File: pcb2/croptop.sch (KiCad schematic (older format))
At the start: 0 parts

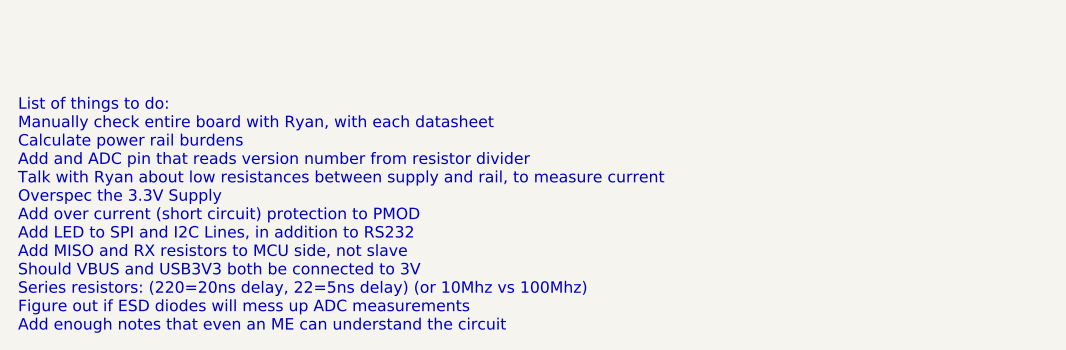
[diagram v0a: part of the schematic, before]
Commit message: Added USB port control
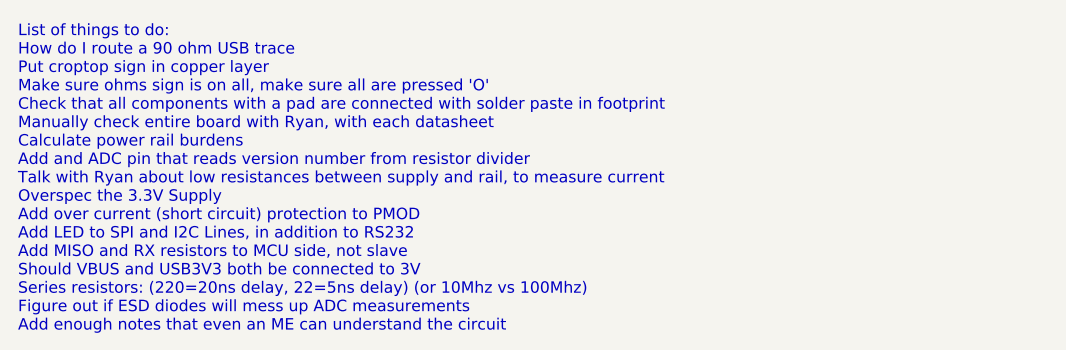
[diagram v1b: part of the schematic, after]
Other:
- note added: "List of things to do:\nHow do I route a 90 ohm USB trace\nPut croptop sign in copper layer\nMake sure ohms sign is on all, make sure all are pressed 'O'\nCheck that all components with a pad are connected with solder paste in footprint\nManually check entire board with Ryan, with each datasheet\nCalculate power rail burdens\nAdd and ADC pin that reads version number from resistor divider\nTalk wi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"
- note removed: "List of things to do:\nManually check entire board with Ryan, with each datasheet\nCalculate power rail burdens\nAdd and ADC pin that reads version number from resistor divider\nTalk with Ryan about low resistances between supply and rail, to measure current\nOverspec the 3.3V Supply\nAdd over current (short circuit) protection to PMOD\nAdd LED to SPI and I2C Lines, in addition to RS232\nAdd MISO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"
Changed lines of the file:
@@
 System Block Diagram
 Text Notes 1250 7850 0    50   ~ 0
-List of things to do:\nManually check entire board with Ryan, with each datasheet\nCalculate power rail burdens\nAdd and ADC pin that reads version number from resistor divider\nTalk with Ryan about low resistances between supply and rail, to measure current\nOverspec the 3.3V Supply\nAdd over current (short circuit) protection to PMOD\nAdd LED to SPI and I2C Lines, in addition to RS232\nAdd MISO and RX resistors to MCU side, not slave\nShould VBUS and USB3V3 both be connected to 3V\nSeries resistors: (220=20ns delay, 22=5ns delay) (or 10Mhz vs 100Mhz)\nFigure out if ESD diodes will mess up ADC measurements\nAdd enough notes that even an ME can understand the circuit\n\nImplement all 4 types of protection:\nReverse polarity protection: PMOS\nFOLLOW PCB Layout tips (temp, GPS, etc)\nAdd a ground pour to empty planes\nESD protection: TVS diodes\nOvervoltage protection: Buffers and schokttky diodes\nOvercurrent protection: PTC fuses AND eFuses\ndv/dt (rise time) protection: series diodes\nRC filters on the input\nLook into Chris Gammel's powerpoint for more info\n\nCome up with different devices configurations (using DNP for components)\n5 Terminal block pins were used for each force sensor\nDoes DRV_FLT need a pull up?\nLook into thermal vias for motor drivers\nAdd silkscreen labels to configuration resistors\nAdd address of components to sheet\nMore protection on motor and stepper? (Stepper pg. 15)\nMake location of resistor value consistent (inside vs. outside)\nMake sure all devices have testpoint in any useful places\nWhen laying out the footprint for the motor drivers, follow datasheet\nRe add isolation dotted box around ADI ADC\nRemove electrolytic input on DC motor driver\nChange AVDD to 5V0_REG, DVDD to 3V3\nAdd inductor to ADC\nChange nets to have directions\nRemove global nets on power\nAdd missing pullups and pulldowns on temp/memory\nAdd MISO to SPI bus\nAdd resistor to Load bank for current limit\nMake board larger at top, add header blocks\nRemove electrolytic input on DC motor driver\nChange AVDD to 5V0_REG, DVDD to 3V3\nCheck regulators can carry high current\nMove micro usb and lcd connector further forward\nSplit memory and adc spi bus\nFlip direction of motor diode\nMap out extra I2C and SPI busses to terminal blocks\nAdd a stepper motor driver\nAdd heat sinks to motor drivers\nRun through pin out of every chip and verify it's connection\nVerify the package footprint of every chip\nAdd ground plane to top and bottom layers\nStitch top and bottom layers together with vias\nAdd pullup resistors/pulldown resistors to data lines\nAdd a second USB port\nAdd a USB switch: USB2422\nAdd a UART to USB coverter: FT232RQ\nAdd LEDs to communication channels\nAdd Series resistors to comm lines, allowing the resistor to be changed\nAdd A4988 stepper motor driver\nAdd GPIO Block with ESD protection\nAdd SPI/UART/I2C with ESD potection on terminal blocks\nAdd labels to terminal blocks, on underside\nThroughole USB\nGround plane on top and bottom layer\nAdd configurable voltage to IO ports\nMove testpoints onto schematic\nPut I2C address on I2C chips\nMake sure all global nets are facing right direciton\nMake sure all LED resistors are selected\nSPI I2C and RS232 testpoints should be closer to pic, or at fork point\nCheck if DC and Stepper motor needs external flyback diodes\nAll elements that have a pad, make sure that there is a pad pin and it's footprint is has the pad assigned to it\nMake sure all CAP on motor drivers are at least 50V Rated\nChange name of I2C and SPI and RS232 to add numbers and what bus? (tx -> I2C_TX_1)\nMove memory and ADC to different busses\nAdd datasheets for components into schematic\nMake sure that 3V3 rotary encoder buffer resistor is DNP\nLabel Terminal blocks on top side\nChange accellerometer to gyro L3GD20H\nRemove buffer from ADC\nMove ADC over star ground\nFigure out whether off board peripherals need buffer\nGive all devices a 10uF and 0.1uF (100nF) capacitor, at the very least\nCan Stepper motor driver use 3.3V for REF?\nAdd an audio circuit to the FTDI chip (recommends TPA6205A1)\nMove ADC and NAND to different SPI Buses\nMake NAND 1GB instead of 1Gb\n\n\n\n
+List of things to do:\nHow do I route a 90 ohm USB trace\nPut croptop sign in copper layer\nMake sure ohms sign is on all, make sure all are pressed 'O'\nCheck that all components with a pad are connected with solder paste in footprint\nManually check entire board with Ryan, with each datasheet\nCalculate power rail burdens\nAdd and ADC pin that reads version number from resistor divider\nTalk with Ryan about low resistances between supply and rail, to measure current\nOverspec the 3.3V Supply\nAdd over current (short circuit) protection to PMOD\nAdd LED to SPI and I2C Lines, in addition to RS232\nAdd MISO and RX resistors to MCU side, not slave\nShould VBUS and USB3V3 both be connected to 3V\nSeries resistors: (220=20ns delay, 22=5ns delay) (or 10Mhz vs 100Mhz)\nFigure out if ESD diodes will mess up ADC measurements\nAdd enough notes that even an ME can understand the circuit\n\nImplement all 4 types of protection:\nReverse polarity protection: PMOS\nFOLLOW PCB Layout tips (temp, GPS, etc)\nAdd a ground pour to empty planes\nESD protection: TVS diodes\nOvervoltage protection: Buffers and schokttky diodes\nOvercurrent protection: PTC fuses AND eFuses\ndv/dt (rise time) protection: series diodes\nRC filters on the input\nLook into Chris Gammel's powerpoint for more info\n\nCome up with different devices configurations (using DNP for components)\n5 Terminal block pins were used for each force sensor\nDoes DRV_FLT need a pull up?\nLook into thermal vias for motor drivers\nAdd silkscreen labels to configuration resistors\nAdd address of components to sheet\nMore protection on motor and stepper? (Stepper pg. 15)\nMake location of resistor value consistent (inside vs. outside)\nMake sure all devices have testpoint in any useful places\nWhen laying out the footprint for the motor drivers, follow datasheet\nRe add isolation dotted box around ADI ADC\nRemove electrolytic input on DC motor driver\nChange AVDD to 5V0_REG, DVDD to 3V3\nAdd inductor to ADC\nChange nets to have directions\nRemove global nets on power\nAdd missing pullups and pulldowns on temp/memory\nAdd MISO to SPI bus\nAdd resistor to Load bank for current limit\nMake board larger at top, add header blocks\nRemove electrolytic input on DC motor driver\nChange AVDD to 5V0_REG, DVDD to 3V3\nCheck regulators can carry high current\nMove micro usb and lcd connector further forward\nSplit memory and adc spi bus\nFlip direction of motor diode\nMap out extra I2C and SPI busses to terminal blocks\nAdd a stepper motor driver\nAdd heat sinks to motor drivers\nRun through pin out of every chip and verify it's connection\nVerify the package footprint of every chip\nAdd ground plane to top and bottom layers\nStitch top and bottom layers together with vias\nAdd pullup resistors/pulldown resistors to data lines\nAdd a second USB port\nAdd a USB switch: USB2422\nAdd a UART to USB coverter: FT232RQ\nAdd LEDs to communication channels\nAdd Series resistors to comm lines, allowing the resistor to be changed\nAdd A4988 stepper motor driver\nAdd GPIO Block with ESD protection\nAdd SPI/UART/I2C with ESD potection on terminal blocks\nAdd labels to terminal blocks, on underside\nThroughole USB\nGround plane on top and bottom layer\nAdd configurable voltage to IO ports\nMove testpoints onto schematic\nPut I2C address on I2C chips\nMake sure all global nets are facing right direciton\nMake sure all LED resistors are selected\nSPI I2C and RS232 testpoints should be closer to pic, or at fork point\nCheck if DC and Stepper motor needs external flyback diodes\nAll elements that have a pad, make sure that there is a pad pin and it's footprint is has the pad assigned to it\nMake sure all CAP on motor drivers are at least 50V Rated\nChange name of I2C and SPI and RS232 to add numbers and what bus? (tx -> I2C_TX_1)\nMove memory and ADC to different busses\nAdd datasheets for components into schematic\nMake sure that 3V3 rotary encoder buffer resistor is DNP\nLabel Terminal blocks on top side\nChange accellerometer to gyro L3GD20H\nRemove buffer from ADC\nMove ADC over star ground\nFigure out whether off board peripherals need buffer\nGive all devices a 10uF and 0.1uF (100nF) capacitor, at the very least\nCan Stepper motor driver use 3.3V for REF?\nAdd an audio circuit to the FTDI chip (recommends TPA6205A1)\nMove ADC and NAND to different SPI Buses\nMake NAND 1GB instead of 1Gb\n\n\n\n
 $Sheet
 S 7700 5150 1200 900

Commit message: Schematic near completion
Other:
- note added: "SCHEMATIC:\nShould Power rails be software or hardware enabled?\nMake sure ohms sign is on all, make sure all are pressed 'O'\nAdd and ADC pin that reads version number from resistor divider\nTalk with Ryan about low resistances between supply and rail, to measure current\nOverspec the 3.3V Supply\nAdd over current (short circuit) protection to PMOD\nAdd LED to SPI and I2C Lines, in addition to R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"
- note removed: "List of things to do:\nHow do I route a 90 ohm USB trace\nPut croptop sign in copper layer\nMake sure ohms sign is on all, make sure all are pressed 'O'\nCheck that all components with a pad are connected with solder paste in footprint\nManually check entire board with Ryan, with each datasheet\nCalculate power rail burdens\nAdd and ADC pin that reads version number from resistor divider\nTalk wi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"
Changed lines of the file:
@@
 $Descr USLetter 11000 8500
 encoding utf-8
-Sheet 1 7
+Sheet 1 6
 Title "CropTop"
 Date "2018-11-20"
@@
 System Block Diagram
 Text Notes 1250 7850 0    50   ~ 0
-List of things to do:\nHow do I route a 90 ohm USB trace\nPut croptop sign in copper layer\nMake sure ohms sign is on all, make sure all are pressed 'O'\nCheck that all components with a pad are connected with solder paste in footprint\nManually check entire board with Ryan, with each datasheet\nCalculate power rail burdens\nAdd and ADC pin that reads version number from resistor divider\nTalk with Ryan about low resistances between supply and rail, to measure current\nOverspec the 3.3V Supply\nAdd over current (short circuit) protection to PMOD\nAdd LED to SPI and I2C Lines, in addition to RS232\nAdd MISO and RX resistors to MCU side, not slave\nShould VBUS and USB3V3 both be connected to 3V\nSeries resistors: (220=20ns delay, 22=5ns delay) (or 10Mhz vs 100Mhz)\nFigure out if ESD diodes will mess up ADC measurements\nAdd enough notes that even an ME can understand the circuit\n\nImplement all 4 types of protection:\nReverse polarity protection: PMOS\nFOLLOW PCB Layout tips (temp, GPS, etc)\nAdd a ground pour to empty planes\nESD protection: TVS diodes\nOvervoltage protection: Buffers and schokttky diodes\nOvercurrent protection: PTC fuses AND eFuses\ndv/dt (rise time) protection: series diodes\nRC filters on the input\nLook into Chris Gammel's powerpoint for more info\n\nCome up with different devices configurations (using DNP for components)\n5 Terminal block pins were used for each force sensor\nDoes DRV_FLT need a pull up?\nLook into thermal vias for motor drivers\nAdd silkscreen labels to configuration resistors\nAdd address of components to sheet\nMore protection on motor and stepper? (Stepper pg. 15)\nMake location of resistor value consistent (inside vs. outside)\nMake sure all devices have testpoint in any useful places\nWhen laying out the footprint for the motor drivers, follow datasheet\nRe add isolation dotted box around ADI ADC\nRemove electrolytic input on DC motor driver\nChange AVDD to 5V0_REG, DVDD to 3V3\nAdd inductor to ADC\nChange nets to have directions\nRemove global nets on power\nAdd missing pullups and pulldowns on temp/memory\nAdd MISO to SPI bus\nAdd resistor to Load bank for current limit\nMake board larger at top, add header blocks\nRemove electrolytic input on DC motor driver\nChange AVDD to 5V0_REG, DVDD to 3V3\nCheck regulators can carry high current\nMove micro usb and lcd connector further forward\nSplit memory and adc spi bus\nFlip direction of motor diode\nMap out extra I2C and SPI busses to terminal blocks\nAdd a stepper motor driver\nAdd heat sinks to motor drivers\nRun through pin out of every chip and verify it's connection\nVerify the package footprint of every chip\nAdd ground plane to top and bottom layers\nStitch top and bottom layers together with vias\nAdd pullup resistors/pulldown resistors to data lines\nAdd a second USB port\nAdd a USB switch: USB2422\nAdd a UART to USB coverter: FT232RQ\nAdd LEDs to communication channels\nAdd Series resistors to comm lines, allowing the resistor to be changed\nAdd A4988 stepper motor driver\nAdd GPIO Block with ESD protection\nAdd SPI/UART/I2C with ESD potection on terminal blocks\nAdd labels to terminal blocks, on underside\nThroughole USB\nGround plane on top and bottom layer\nAdd configurable voltage to IO ports\nMove testpoints onto schematic\nPut I2C address on I2C chips\nMake sure all global nets are facing right direciton\nMake sure all LED resistors are selected\nSPI I2C and RS232 testpoints should be closer to pic, or at fork point\nCheck if DC and Stepper motor needs external flyback diodes\nAll elements that have a pad, make sure that there is a pad pin and it's footprint is has the pad assigned to it\nMake sure all CAP on motor drivers are at least 50V Rated\nChange name of I2C and SPI and RS232 to add numbers and what bus? (tx -> I2C_TX_1)\nMove memory and ADC to different busses\nAdd datasheets for components into schematic\nMake sure that 3V3 rotary encoder buffer resistor is DNP\nLabel Terminal blocks on top side\nChange accellerometer to gyro L3GD20H\nRemove buffer from ADC\nMove ADC over star ground\nFigure out whether off board peripherals need buffer\nGive all devices a 10uF and 0.1uF (100nF) capacitor, at the very least\nCan Stepper motor driver use 3.3V for REF?\nAdd an audio circuit to the FTDI chip (recommends TPA6205A1)\nMove ADC and NAND to different SPI Buses\nMake NAND 1GB instead of 1Gb\n\n\n\n
-$Sheet
-S 7700 5150 1200 900
-U 5EC973C3
-F0 "Connectors" 50
-F1 "croptop_conn.sch" 50
-$EndSheet
+SCHEMATIC:\nShould Power rails be software or hardware enabled?\nMake sure ohms sign is on all, make sure all are pressed 'O'\nAdd and ADC pin that reads version number from resistor divider\nTalk with Ryan about low resistances between supply and rail, to measure current\nOverspec the 3.3V Supply\nAdd over current (short circuit) protection to PMOD\nAdd LED to SPI and I2C Lines, in addition to RS232\nAdd MISO and RX resistors to MCU side, not slave\nShould VBUS and USB3V3 both be connected to 3V\nThroughole USB\nAdd pullup resistors/pulldown resistors to data lines\nAdd a second USB port\nAdd a USB switch: USB2422\nAdd a UART to USB coverter: FT232RQ\nAdd LEDs to communication channels\nAdd Series resistors to comm lines, allowing the resistor to be changed\nAdd A4988 stepper motor driver\nAdd GPIO Block with ESD protection\nAdd SPI/UART/I2C with ESD potection on terminal blocks\nAdd a stepper motor driver\nAdd an audio circuit to the FTDI chip (recommends TPA6205A1)\nAdd enough notes that even an ME can understand the circuit\nAdd missing pullups and pulldowns on temp/memory\nAdd MISO to SPI bus\nAdd resistor to Load bank for current limit\nSeries resistors: (220=20ns delay, 22=5ns delay) (or 10Mhz vs 100Mhz)\nAdd address of components to sheet\nMore protection on motor and stepper? (Stepper pg. 15)\nMake location of resistor value consistent (inside vs. outside)\nMake sure all devices have testpoint in any useful places\nChange AVDD to 5V0_REG, DVDD to 3V3\nAdd inductor to ADC\nChange nets to have directions\nRemove global nets on power\nSplit memory and adc spi bus\nAdd datasheets for components into schematic\nAdd configurable voltage to IO ports\nMove testpoints onto schematic\nMake sure all global nets are facing right direciton\nMake sure all LED resistors are selected\nDoes DRV_FLT need a pull up?\nCheck if DC and Stepper motor needs external flyback diodes\nChange accellerometer to gyro L3GD20H\nRemove buffer from ADC\nFigure out whether off board peripherals need buffer\nMake sure all CAP on motor drivers are at least 50V Rated\nCan Stepper motor driver use 3.3V for REF?\nChange name of I2C and SPI and RS232 to add numbers and what bus? (tx -> I2C_TX_1)\nMove ADC and NAND to different SPI Buses\nMake NAND 1GB instead of 1Gb\nFillout partnumber and datasheet for all components\nGive all devices a 10uF and 0.1uF (100nF) capacitor, at the very least\n\nPCB:\nAll elements that have a pad, make sure that there is a pad pin and it's footprint is has the pad assigned to it\nCheck that all components with a pad are connected with solder paste in footprint\nAdd a cut out around temperature sensor\nAdd vias to mounting holes for style\nMake logo in copper layer, not silkscreen\nHow do I route a 90 ohm USB trace\nPut croptop sign in copper layer\nMove ADC over star ground\nMove memory and ADC to different busses\nAdd heat sinks to motor drivers\nGround plane on top and bottom layer\nLook into thermal vias for motor drivers\nAdd silkscreen labels to configuration resistors\nWhen laying out the footprint for the motor drivers, follow datasheet\nMove micro usb and lcd connector further forward\nAdd ground plane to top and bottom layers\nStitch top and bottom layers together with vias\nSPI I2C and RS232 testpoints should be closer to pic, or at fork point\nLabel Terminal blocks on top side\n\nCOMPLETION STEPS:\nManually check entire board with Ryan, with each datasheet\nCalculate power rail burdens\nFigure out if ESD diodes will mess up ADC measurements\nCome up with different devices configurations (using DNP for components)\nRun through pin out of every chip and verify it's connection\nVerify the package footprint of every chip\nMake sure that 3V3 rotary encoder buffer resistor is DNP\n
 $EndSCHEMATC
